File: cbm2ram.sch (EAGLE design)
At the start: 10 parts, among them IC2 HM628512A_DIL32, IC3 HM628512A_DIL32, IC4 GAL16V8

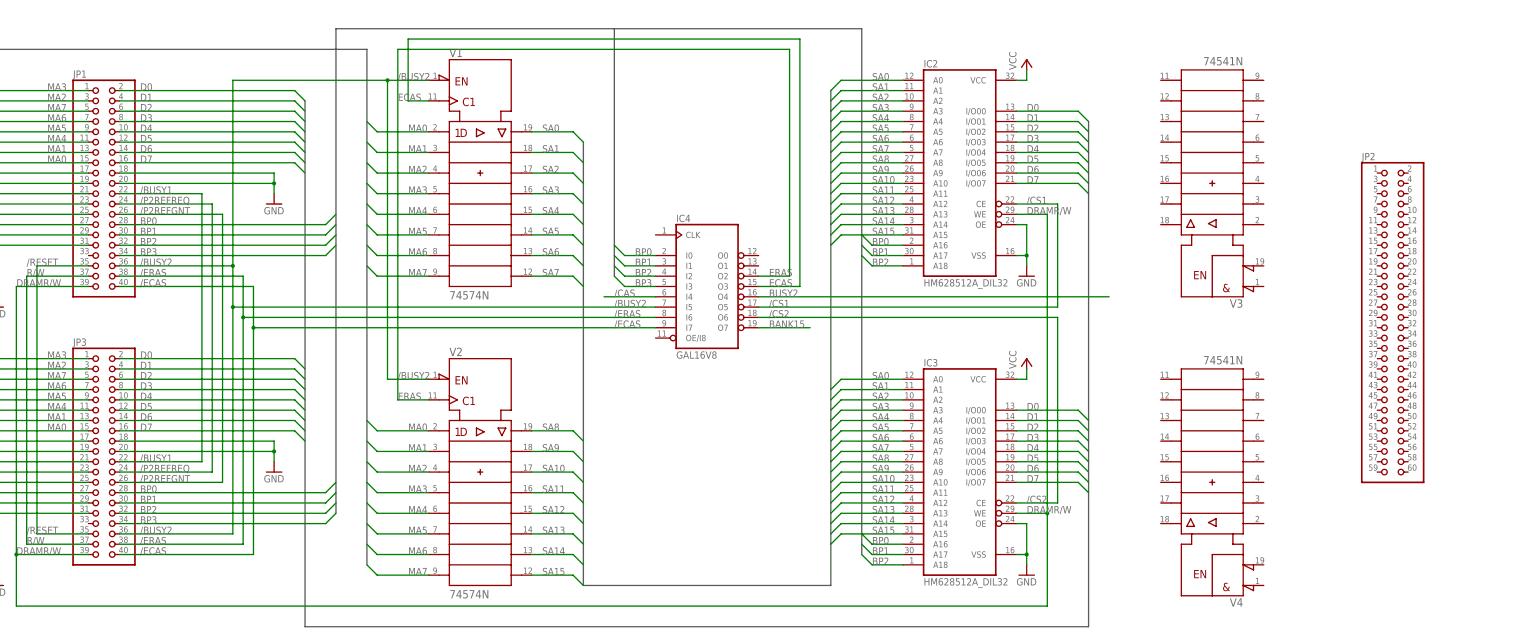
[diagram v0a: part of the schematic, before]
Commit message: Schematic of the 6509 interface
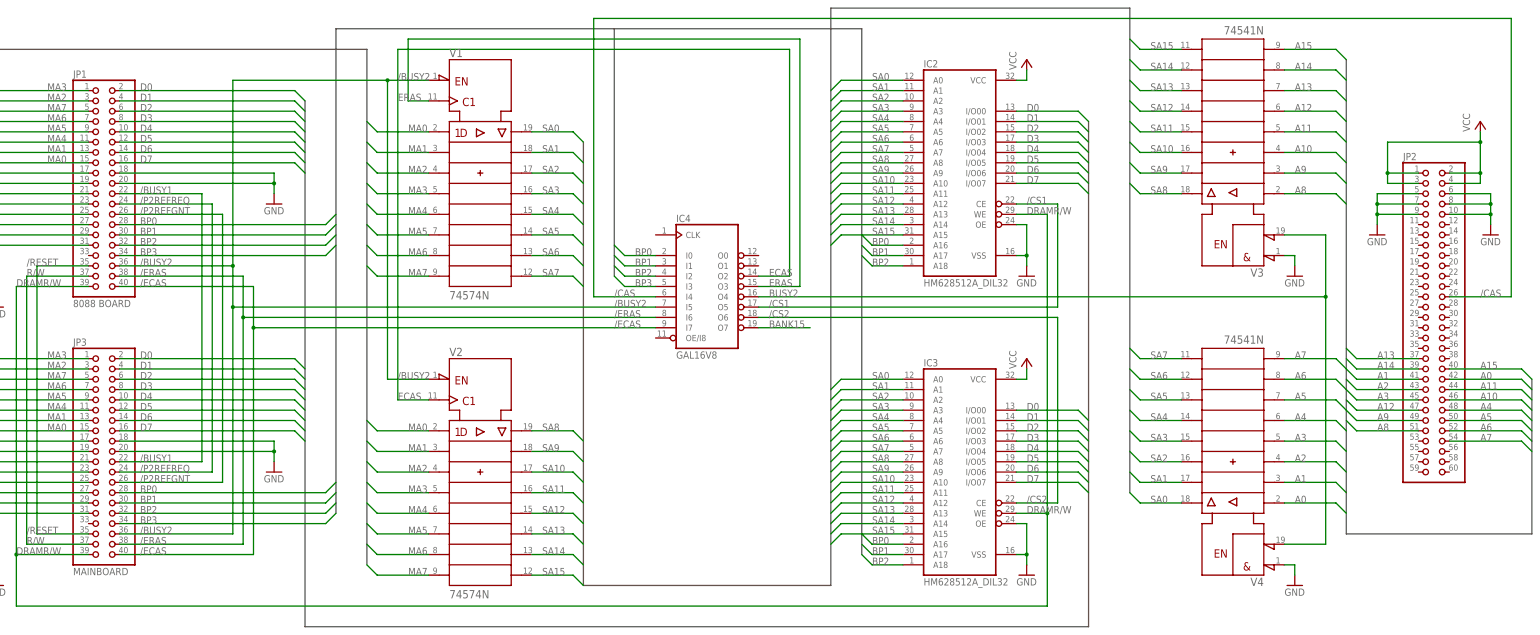
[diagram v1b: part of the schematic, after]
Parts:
- JP1: value (none) -> 8088 BOARD
- JP3: value (none) -> MAINBOARD
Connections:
- new net A0: JP2.42, V41.A1
- new net A1: JP2.41, V41.A2
- new net A10: JP2.46, V31.A3
- new net A11: JP2.44, V31.A4
- new net A12: JP2.47, V31.A5
- new net A13: JP2.37, V31.A6
- new net A14: JP2.39, V31.A7
- new net A15: JP2.40, V31.A8
- new net A2: JP2.43, V41.A3
- new net A3: JP2.45, V41.A4
- new net A4: JP2.48, V41.A5
- new net A5: JP2.50, V41.A6
- new net A6: JP2.52, V41.A7
- new net A7: JP2.54, V41.A8
- new net A8: JP2.51, V31.A1
- new net A9: JP2.49, V31.A2
- net /CAS: now also JP2.26
- net BUSY2: now also V31.!G2, V41.!G2
- net ECAS: now also IC4G$1.O2, V21.CLK; no longer IC4G$1.O3, V11.CLK
- net ERAS: now also IC4G$1.O3, V11.CLK; no longer IC4G$1.O2, V21.CLK
- net GND: now also JP2.10, JP2.5, JP2.6, JP2.7, JP2.8, JP2.9, V31.!G1, V41.!G1
- net SA0: now also V41.Y1
- net SA1: now also V41.Y2
- net SA10: now also V31.Y3
- net SA11: now also V31.Y4
- net SA12: now also V31.Y5
- net SA13: now also V31.Y6
- net SA14: now also V31.Y7
- net SA15: now also V31.Y8
- net SA2: now also V41.Y3
- net SA3: now also V41.Y4
- net SA4: now also V41.Y5
- net SA5: now also V41.Y6
- net SA6: now also V41.Y7
- net SA7: now also V41.Y8
- net SA8: now also V31.Y1
- net SA9: now also V31.Y2
- net VCC: now also JP2.1, JP2.2, JP2.3, JP2.4
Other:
- moved on the sheet: JP2, V3, V4

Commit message: Complete schematic
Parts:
- removed JP2: (no value), pinhead:PINHD-2X30
- removed V3, V4: 74541N, 74ttl-din:74541N
- added CONN1: (no value), pinhead:PINHD-2X20/90
- added CONN3: (no value), pinhead:PINHD-2X30
- added R1: (no value), resistor:R-EU_0207/10
- added U4: 74LS04N, 74xx-eu:74LS04N
- added U7, U8: 74541N, 74ttl-din:74541N
- CONN2: value MAINBOARD -> (none)
- JP1: value 8088 BOARD -> (none); device pinhead:PINHD-2X20/90 -> jumper:JP1E
- renumbered IC2 to U5, IC3 to U6, IC4 to U3, JP3 to CONN2, V1 to U1, V2 to U2
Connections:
- new net N$1: JP1.1, R1.1, U3G$1.I6
- net /BUSY1: now also CONN1.22; no longer JP1.22
- net /BUSY2: now also CONN1.36, U4C.I; no longer JP1.36
- net /CAS: now also CONN3.26; no longer JP2.26
- net /ECAS: now also CONN1.40, U4B.I; no longer JP1.40
- net /ERAS: now also CONN1.38, U4A.I; no longer JP1.38, U3G$1.I6
- net /P2REFGNT: now also CONN1.26; no longer JP1.26
- net /P2REFREQ: now also CONN1.24; no longer JP1.24
- net /RESET: now also CONN1.35; no longer JP1.35
- net A0: now also CONN3.42, U71.A8; no longer JP2.42, V41.A1
- net A1: now also CONN3.41, U71.A7; no longer JP2.41, V41.A2
- net A10: now also CONN3.46, U81.A6; no longer JP2.46, V31.A3
- net A11: now also CONN3.44, U81.A5; no longer JP2.44, V31.A4
- net A12: now also CONN3.47, U81.A4; no longer JP2.47, V31.A5
- net A13: now also CONN3.37, U81.A3; no longer JP2.37, V31.A6
- net A14: now also CONN3.39, U81.A2; no longer JP2.39, V31.A7
- net A15: now also CONN3.40, U81.A1; no longer JP2.40, V31.A8
- net A2: now also CONN3.43, U71.A6; no longer JP2.43, V41.A3
- net A3: now also CONN3.45, U71.A5; no longer JP2.45, V41.A4
- net A4: now also CONN3.48, U71.A4; no longer JP2.48, V41.A5
- net A5: now also CONN3.50, U71.A3; no longer JP2.50, V41.A6
- net A6: now also CONN3.52, U71.A2; no longer JP2.52, V41.A7
- net A7: now also CONN3.54, U71.A1; no longer JP2.54, V41.A8
- net A8: now also CONN3.51, U81.A8; no longer JP2.51, V31.A1
- net A9: now also CONN3.49, U81.A7; no longer JP2.49, V31.A2
- net BP0: now also CONN1.28; no longer JP1.28
- net BP1: now also CONN1.30; no longer JP1.30
- net BP2: now also CONN1.32; no longer JP1.32
- net BP3: now also CONN1.34; no longer JP1.34
- net BUSY2: now also U4C.O, U71.!G1, U71.!G2, U81.!G1, U81.!G2; no longer U3G$1.O4, V31.!G2, V41.!G2
- net D0: now also CONN1.2; no longer JP1.2
- net D1: now also CONN1.4; no longer JP1.4
- net D2: now also CONN1.6; no longer JP1.6
- net D3: now also CONN1.8; no longer JP1.8
- net D4: now also CONN1.10; no longer JP1.10
- net D5: now also CONN1.12; no longer JP1.12
- net D6: now also CONN1.14; no longer JP1.14
- net D7: now also CONN1.16; no longer JP1.16
- net DRAMR/W: now also CONN1.39; no longer JP1.39
- net ECAS: now also U11.CLK, U4B.O; no longer U21.CLK, U3G$1.O2
- net ERAS: now also U21.CLK, U4A.O; no longer U11.CLK, U3G$1.O3
- net GND: now also CONN1.17, CONN1.18, CONN1.19, CONN1.20, CONN1.21, CONN1.23, CONN1.25, CONN1.27, CONN1.29, CONN1.31, CONN3.10, CONN3.5, CONN3.6, CONN3.7, CONN3.8, CONN3.9, JP1.2; no longer JP1.17, JP1.18, JP1.19, JP1.20, JP1.21, JP1.23, JP1.25, JP1.27, JP1.29, JP1.31, JP2.10, JP2.5, JP2.6, JP2.7, JP2.8, JP2.9, V31.!G1, V41.!G1
- net MA0: now also CONN1.15; no longer JP1.15
- net MA1: now also CONN1.13; no longer JP1.13
- net MA2: now also CONN1.3; no longer JP1.3
- net MA3: now also CONN1.1; no longer JP1.1
- net MA4: now also CONN1.11; no longer JP1.11
- net MA5: now also CONN1.9; no longer JP1.9
- net MA6: now also CONN1.7; no longer JP1.7
- net MA7: now also CONN1.5; no longer JP1.5
- net R/W: now also CONN1.37; no longer JP1.37
- net SA0: now also U71.Y8; no longer V41.Y1
- net SA1: now also U71.Y7; no longer V41.Y2
- net SA10: now also U81.Y6; no longer V31.Y3
- net SA11: now also U81.Y5; no longer V31.Y4
- net SA12: now also U81.Y4; no longer V31.Y5
- net SA13: now also U81.Y3; no longer V31.Y6
- net SA14: now also U81.Y2; no longer V31.Y7
- net SA15: now also U81.Y1; no longer V31.Y8
- net SA2: now also U71.Y6; no longer V41.Y3
- net SA3: now also U71.Y5; no longer V41.Y4
- net SA4: now also U71.Y4; no longer V41.Y5
- net SA5: now also U71.Y3; no longer V41.Y6
- net SA6: now also U71.Y2; no longer V41.Y7
- net SA7: now also U71.Y1; no longer V41.Y8
- net SA8: now also U81.Y8; no longer V31.Y1
- net SA9: now also U81.Y7; no longer V31.Y2
- net VCC: now also CONN3.1, CONN3.2, CONN3.3, CONN3.4, R1.2; no longer JP2.1, JP2.2, JP2.3, JP2.4

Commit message: Schematic corrections
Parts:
- added C1, C2, C3, C4, C5, C6, C7, C8: 330n, capacitor-wima:C5/3
- CONN1, CONN2: device pinhead:PINHD-2X20/90 -> pinhead:PINHD-2X20
- R1: value (none) -> 5.1k
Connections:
- net GND: now also C1.2, C8.2, U1/-UB.-UB, U2/-UB.-UB, U7/-UB.-UB, U8/-UB.-UB
- net VCC: now also C1.1, C8.1, U1/+UB.+UB, U2/+UB.+UB, U7/+UB.+UB, U8/+UB.+UB
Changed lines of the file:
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@@
 <part name="U7" library="74ttl-din" deviceset="74*541" device="N"/>
 <part name="U8" library="74ttl-din" deviceset="74*541" device="N"/>
-<part name="CONN1" library="pinhead" deviceset="PINHD-2X20" device="/90"/>
-<part name="CONN2" library="pinhead" deviceset="PINHD-2X20" device="/90"/>
+<part name="CONN1" library="pinhead" deviceset="PINHD-2X20" device=""/>
+<part name="CONN2" library="pinhead" deviceset="PINHD-2X20" device=""/>
 <part name="U4" library="74xx-eu" deviceset="74*04" device="N" technology="LS"/>
 <part name="P+3" library="supply1" deviceset="VCC" device=""/>
@@
 <part name="JP1" library="jumper" deviceset="JP1E" device=""/>
 <part name="GND9" library="supply1" deviceset="GND" device=""/>
-<part name="R1" library="resistor" deviceset="R-EU_" device="0207/10"/>
+<part name="R1" library="resistor" deviceset="R-EU_" device="0207/10" value="5.1k"/>
 <part name="P+4" library="supply1" deviceset="VCC" device=""/>
+<part name="P+5" library="supply1" deviceset="VCC" device=""/>
+<part name="P+6" library="supply1" deviceset="VCC" device=""/>
+<part name="GND10" library="supply1" deviceset="GND" device=""/>
+<part name="GND11" library="supply1" deviceset="GND" device=""/>
+<part name="P+7" library="supply1" deviceset="VCC" device=""/>
+<part name="GND12" library="supply1" deviceset="GND" device=""/>
+<part name="P+8" library="supply1" deviceset="VCC" device=""/>
+<part name="GND13" library="supply1" deviceset="GND" device=""/>
+<part name="C1" library="capacitor-wima" deviceset="C" device="5/3" value="330n"/>
+<part name="C2" library="capacitor-wima" deviceset="C" device="5/3" value="330n"/>
+<part name="C3" library="capacitor-wima" deviceset="C" device="5/3" value="330n"/>
+<part name="C4" library="capacitor-wima" deviceset="C" device="5/3" value="330n"/>
+<part name="C5" library="capacitor-wima" deviceset="C" device="5/3" value="330n"/>
+<part name="C6" library="capacitor-wima" deviceset="C" device="5/3" value="330n"/>
+<part name="C7" library="capacitor-wima" deviceset="C" device="5/3" value="330n"/>
+<part name="C8" library="capacitor-wima" deviceset="C" device="5/3" value="330n"/>
+<part name="P+9" library="supply1" deviceset="VCC" device=""/>
+<part name="GND14" library="supply1" deviceset="GND" device=""/>
 </parts>
 <sheets>
@@
 <instance part="R1" gate="G$1" x="83.82" y="101.6" rot="R90"/>
 <instance part="P+4" gate="VCC" x="83.82" y="109.22"/>
+<instance part="U1" gate="/+UB" x="63.5" y="109.22"/>
+<instance part="P+5" gate="VCC" x="63.5" y="114.3"/>
+<instance part="U2" gate="/+UB" x="58.42" y="45.72"/>
+<instance part="P+6" gate="VCC" x="58.42" y="50.8"/>
+<instance part="U1" gate="/-UB" x="55.88" y="116.84"/>
+<instance part="GND10" gate="1" x="55.88" y="111.76"/>
+<instance part="U2" gate="/-UB" x="58.42" y="40.64"/>
+<instance part="GND11" gate="1" x="58.42" y="35.56"/>
+<instance part="U7" gate="/+UB" x="208.28" y="71.12"/>
+<instance part="P+7" gate="VCC" x="208.28" y="76.2"/>
+<instance part="U7" gate="/-UB" x="208.28" y="66.04"/>
+<instance part="GND12" gate="1" x="208.28" y="60.96"/>
+<instance part="U8" gate="/+UB" x="208.28" y="-2.54"/>
+<instance part="U8" gate="/-UB" x="208.28" y="-7.62"/>
+<instance part="P+8" gate="VCC" x="208.28" y="2.54"/>
+<instance part="GND13" gate="1" x="208.28" y="-12.7"/>
+<instance part="C1" gate="G$1" x="-71.12" y="142.24"/>
+<instance part="C2" gate="G$1" x="-63.5" y="142.24"/>
+<instance part="C3" gate="G$1" x="-55.88" y="142.24"/>
+<instance part="C4" gate="G$1" x="-48.26" y="142.24"/>
+<instance part="C5" gate="G$1" x="-40.64" y="142.24"/>
+<instance part="C6" gate="G$1" x="-33.02" y="142.24"/>
+<instance part="C7" gate="G$1" x="-25.4" y="142.24"/>
+<instance part="C8" gate="G$1" x="-17.78" y="142.24"/>
+<instance part="P+9" gate="VCC" x="-17.78" y="147.32"/>
+<instance part="GND14" gate="1" x="-17.78" y="134.62"/>
 </instances>
 <busses>
@@
 <pinref part="GND9" gate="1" pin="GND"/>
 </segment>
+<segment>
+<pinref part="U1" gate="/-UB" pin="-UB"/>
+<pinref part="GND10" gate="1" pin="GND"/>
+</segment>
+<segment>
+<pinref part="U2" gate="/-UB" pin="-UB"/>
+<pinref part="GND11" gate="1" pin="GND"/>
+</segment>
+<segment>
+<pinref part="U7" gate="/-UB" pin="-UB"/>
+<pinref part="GND12" gate="1" pin="GND"/>
+</segment>
+<segment>
+<pinref part="U8" gate="/-UB" pin="-UB"/>
+<pinref part="GND13" gate="1" pin="GND"/>
+</segment>
+<segment>
+<pinref part="C8" gate="G$1" pin="2"/>
+<pinref part="C1" gate="G$1" pin="2"/>
+<wire x1="-17.78" y1="137.16" x2="-71.12" y2="137.16" width="0.1524" layer="91"/>
+<pinref part="GND14" gate="1" pin="GND"/>
+<junction x="-17.78" y="137.16"/>
+</segment>
 </net>
 <net name="/BUSY1" class="0">
@@
 <pinref part="P+4" gate="VCC" pin="VCC"/>
 </segment>
-</net>
+<segment>
+<pinref part="U1" gate="/+UB" pin="+UB"/>
+<pinref part="P+5" gate="VCC" pin="VCC"/>
+</segment>
+<segment>
+<pinref part="U2" gate="/+UB" pin="+UB"/>
+<pinref part="P+6" gate="VCC" pin="VCC"/>
+</segment>
+<segment>
+<pinref part="U7" gate="/+UB" pin="+UB"/>
+<pinref part="P+7" gate="VCC" pin="VCC"/>
+</segment>
+<segment>
+<pinref part="U8" gate="/+UB" pin="+UB"/>
+<pinref part="P+8" gate="VCC" pin="VCC"/>
+</segment>
+<segment>
+<pinref part="C1" gate="G$1" pin="1"/>
+<pinref part="C8" gate="G$1" pin="1"/>
+<wire x1="-71.12" y1="144.78" x2="-17.78" y2="144.78" width="0.1524" layer="91"/>
+<pinref part="P+9" gate="VCC" pin="VCC"/>
+<junction x="-17.78" y="144.78"/>
+</segment>
+</net>

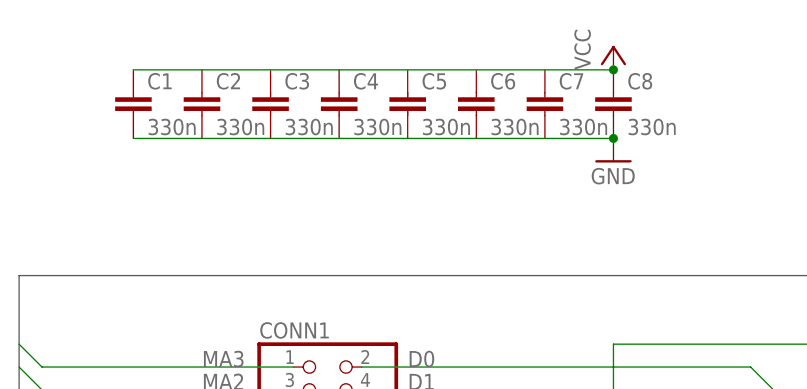
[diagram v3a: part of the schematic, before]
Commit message: Firt autorouted board
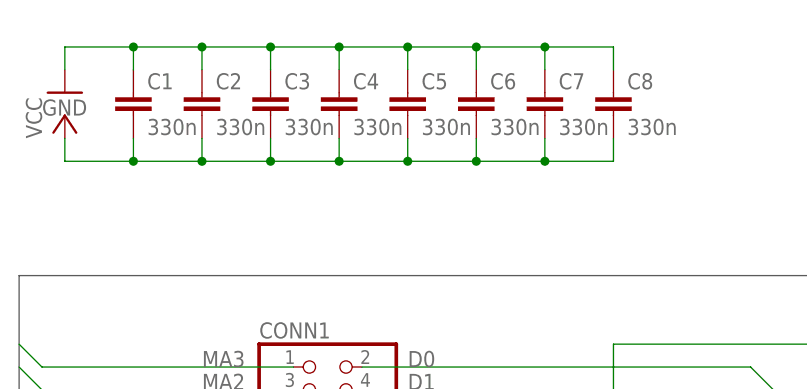
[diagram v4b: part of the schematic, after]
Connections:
- net GND: now also C1.1, C2.1, C3.1, C4.1, C5.1, C6.1, C7.1, C8.1; no longer C1.2, C8.2
- net VCC: now also C1.2, C2.2, C3.2, C4.2, C5.2, C6.2, C7.2, C8.2; no longer C1.1, C8.1
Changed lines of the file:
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@@
 </variantdefs>
 <classes>
-<class number="0" name="default" width="0" drill="0">
+<class number="0" name="default" width="0.2032" drill="0">
+<clearance class="0" value="0.2032"/>
+</class>
+<class number="1" name="power" width="0.4064" drill="0">
+<clearance class="0" value="0.254"/>
+<clearance class="1" value="0.254"/>
 </class>
 </classes>
@@
 <instance part="C7" gate="G$1" x="-25.4" y="142.24"/>
 <instance part="C8" gate="G$1" x="-17.78" y="142.24"/>
-<instance part="P+9" gate="VCC" x="-17.78" y="147.32"/>
-<instance part="GND14" gate="1" x="-17.78" y="134.62"/>
+<instance part="P+9" gate="VCC" x="-78.74" y="139.7"/>
+<instance part="GND14" gate="1" x="-78.74" y="142.24"/>
 </instances>
 <busses>
@@
 </busses>
 <nets>
-<net name="GND" class="0">
+<net name="GND" class="1">
 <segment>
 <pinref part="GND1" gate="1" pin="GND"/>
@@
 </segment>
 <segment>
-<pinref part="C8" gate="G$1" pin="2"/>
-<pinref part="C1" gate="G$1" pin="2"/>
-<wire x1="-17.78" y1="137.16" x2="-71.12" y2="137.16" width="0.1524" layer="91"/>
 <pinref part="GND14" gate="1" pin="GND"/>
-<junction x="-17.78" y="137.16"/>
+<wire x1="-78.74" y1="144.78" x2="-78.74" y2="147.32" width="0.1524" layer="91"/>
+<pinref part="C1" gate="G$1" pin="1"/>
+<pinref part="C8" gate="G$1" pin="1"/>
+<wire x1="-71.12" y1="144.78" x2="-71.12" y2="147.32" width="0.1524" layer="91"/>
+<wire x1="-71.12" y1="147.32" x2="-63.5" y2="147.32" width="0.1524" layer="91"/>
+<wire x1="-63.5" y1="147.32" x2="-55.88" y2="147.32" width="0.1524" layer="91"/>
+<wire x1="-55.88" y1="147.32" x2="-48.26" y2="147.32" width="0.1524" layer="91"/>
+<wire x1="-48.26" y1="147.32" x2="-40.64" y2="147.32" width="0.1524" layer="91"/>
+<wire x1="-40.64" y1="147.32" x2="-33.02" y2="147.32" width="0.1524" layer="91"/>
+<wire x1="-33.02" y1="147.32" x2="-25.4" y2="147.32" width="0.1524" layer="91"/>
+<wire x1="-25.4" y1="147.32" x2="-17.78" y2="147.32" width="0.1524" layer="91"/>
+<wire x1="-17.78" y1="147.32" x2="-17.78" y2="144.78" width="0.1524" layer="91"/>
+<pinref part="C2" gate="G$1" pin="1"/>
+<wire x1="-63.5" y1="144.78" x2="-63.5" y2="147.32" width="0.1524" layer="91"/>
+<junction x="-63.5" y="147.32"/>
+<pinref part="C3" gate="G$1" pin="1"/>
+<wire x1="-55.88" y1="144.78" x2="-55.88" y2="147.32" width="0.1524" layer="91"/>
+<junction x="-55.88" y="147.32"/>
+<pinref part="C4" gate="G$1" pin="1"/>
+<wire x1="-48.26" y1="144.78" x2="-48.26" y2="147.32" width="0.1524" layer="91"/>
+<junction x="-48.26" y="147.32"/>
+<pinref part="C5" gate="G$1" pin="1"/>
+<wire x1="-40.64" y1="144.78" x2="-40.64" y2="147.32" width="0.1524" layer="91"/>
+<junction x="-40.64" y="147.32"/>
+<pinref part="C6" gate="G$1" pin="1"/>
+<wire x1="-33.02" y1="144.78" x2="-33.02" y2="147.32" width="0.1524" layer="91"/>
+<junction x="-33.02" y="147.32"/>
+<pinref part="C7" gate="G$1" pin="1"/>
+<wire x1="-25.4" y1="144.78" x2="-25.4" y2="147.32" width="0.1524" layer="91"/>
+<junction x="-25.4" y="147.32"/>
+<wire x1="-78.74" y1="147.32" x2="-71.12" y2="147.32" width="0.1524" layer="91"/>
+<junction x="-71.12" y="147.32"/>
 </segment>
 </net>
@@
 </segment>
 </net>
-<net name="VCC" class="0">
+<net name="VCC" class="1">
 <segment>
 <pinref part="U5" gate="G$1" pin="VCC"/>
@@
 </segment>
 <segment>
-<pinref part="C1" gate="G$1" pin="1"/>
-<pinref part="C8" gate="G$1" pin="1"/>
-<wire x1="-71.12" y1="144.78" x2="-17.78" y2="144.78" width="0.1524" layer="91"/>
 <pinref part="P+9" gate="VCC" pin="VCC"/>
-<junction x="-17.78" y="144.78"/>
-</segment>
-</net>
+<wire x1="-78.74" y1="137.16" x2="-78.74" y2="134.62" width="0.1524" layer="91"/>
+<pinref part="C8" gate="G$1" pin="2"/>
+<pinref part="C1" gate="G$1" pin="2"/>
+<wire x1="-17.78" y1="134.62" x2="-25.4" y2="134.62" width="0.1524" layer="91"/>
+<wire x1="-25.4" y1="134.62" x2="-33.02" y2="134.62" width="0.1524" layer="91"/>
+<wire x1="-33.02" y1="134.62" x2="-40.64" y2="134.62" width="0.1524" layer="91"/>
+<wire x1="-40.64" y1="134.62" x2="-48.26" y2="134.62" width="0.1524" layer="91"/>
+<wire x1="-48.26" y1="134.62" x2="-55.88" y2="134.62" width="0.1524" layer="91"/>
+<wire x1="-55.88" y1="134.62" x2="-63.5" y2="134.62" width="0.1524" layer="91"/>
+<wire x1="-63.5" y1="134.62" x2="-71.12" y2="134.62" width="0.1524" layer="91"/>
+<wire x1="-71.12" y1="134.62" x2="-71.12" y2="137.16" width="0.1524" layer="91"/>
+<wire x1="-17.78" y1="134.62" x2="-17.78" y2="137.16" width="0.1524" layer="91"/>
+<pinref part="C7" gate="G$1" pin="2"/>
+<wire x1="-25.4" y1="137.16" x2="-25.4" y2="134.62" width="0.1524" layer="91"/>
+<junction x="-25.4" y="134.62"/>
+<pinref part="C6" gate="G$1" pin="2"/>
+<wire x1="-33.02" y1="137.16" x2="-33.02" y2="134.62" width="0.1524" layer="91"/>
+<junction x="-33.02" y="134.62"/>
+<pinref part="C5" gate="G$1" pin="2"/>
+<wire x1="-40.64" y1="137.16" x2="-40.64" y2="134.62" width="0.1524" layer="91"/>
+<junction x="-40.64" y="134.62"/>
+<pinref part="C4" gate="G$1" pin="2"/>
+<wire x1="-48.26" y1="137.16" x2="-48.26" y2="134.62" width="0.1524" layer="91"/>
+<junction x="-48.26" y="134.62"/>
+<pinref part="C3" gate="G$1" pin="2"/>
+<wire x1="-55.88" y1="137.16" x2="-55.88" y2="134.62" width="0.1524" layer="91"/>
+<junction x="-55.88" y="134.62"/>
+<pinref part="C2" gate="G$1" pin="2"/>
+<wire x1="-63.5" y1="137.16" x2="-63.5" y2="134.62" width="0.1524" layer="91"/>
+<junction x="-63.5" y="134.62"/>
+<wire x1="-78.74" y1="134.62" x2="-71.12" y2="134.62" width="0.1524" layer="91"/>
+<junction x="-71.12" y="134.62"/>
+</segment>
+</net>
